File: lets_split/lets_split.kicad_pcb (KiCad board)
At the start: 2 copper layers, 112 x 79 mm, 62 parts, among them J1 3PIN, J2 6PIN, J3 3PIN, SW1 SW_PUSH, SW10 SW_PUSH, SW11 SW_PUSH, SW12 SW_PUSH, SW13 SW_PUSH, SW14 SW_PUSH, SW15 SW_PUSH, SW16 SW_PUSH, SW17 SW_PUSH, SW18 SW_PUSH, SW19 SW_PUSH, SW2 SW_PUSH, SW21 SW_PUSH, SW22 SW_PUSH, SW23 SW_PUSH, SW3 SW_PUSH, SW4 SW_PUSH, SW5 SW_PUSH, SW6 SW_PUSH, SW7 SW_PUSH, SW8 SW_PUSH, SW9 SW_PUSH, U2 HOLE, U3 HOLE, U4 HOLE, U5 HOLE

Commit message: Finished desing
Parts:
- removed ? (x2): SW_PUSH, flipalps:MXALPS_FLIP
- removed U2, U3, U4, U5: HOLE, prettylib:HOLE
- removed W1: TEST, prettylib:JUMPER_SMD_2DUB
- removed W2: TEST_1P, Wire_Pads:SolderWirePad_single_2mmDrill
- added JP1: I2C / Serial, Jumpers:Solder-jumper-NO, B.Cu at (157.6, 71.8)
- added REF**: 1pin, Connect:1pin, F.Cu at (186.2, 74.5)
- added REF**: 1pin, Connect:1pin, F.Cu at (186.3, 112.5)
- added REF**: 1pin, Connect:1pin, F.Cu at (110.0, 112.5)
- added SW20: SW_PUSH, Kailh-socket, F.Cu at (119.5, 122.0)
- added SW24: SW_PUSH, Kailh-socket, F.Cu at (195.8, 122.0)
- J1, J3: footprint prettylib:jumper -> jumper-3pin-smd-dualside
- J2: value 6PIN -> CONN_01X04; footprint footprint:4pin35mmAudio -> Connectors:4ucon-20153; moved to B.Cu
- R1, R2: value R -> 4k7; footprint footprint:RESISTOR -> Resistors_ThroughHole:R_Axial_DIN0207_L6.3mm_D2.5mm_P10.16mm_Horizontal
- SW1, SW10, SW11, SW12, SW13, SW14, SW15, SW16, SW17, SW18, SW19, SW2, SW21, SW22, SW23, SW3, SW4, SW5, SW6, SW7, SW8, SW9: footprint flipalps:MXALPS_FLIP -> Kailh-socket
- U1: value (none) -> ArduinoProMicro; footprint footprint:TEENSY_2.0 -> plug-in-modules:ArduinoProMicro; moved to F.Cu
- moved SW6 131.2 mm to (195.8, 64.8), turned to 180 degrees
- moved SW4 118.8 mm to (157.7, 64.8)
- moved SW12 113.9 mm to (195.8, 83.9), turned to 180 degrees
- moved SW5 113.6 mm to (176.7, 64.8), turned to 180 degrees
- moved SW3 95.3 mm to (138.6, 64.8)
- moved SW11 93.1 mm to (176.7, 83.9), turned to 180 degrees
- moved SW18 82.8 mm to (195.8, 103.0), turned to 180 degrees
- moved SW17 78.6 mm to (176.7, 103.0), turned to 180 degrees
- moved SW10 76.2 mm to (157.7, 83.9)
- moved SW21 75.2 mm to (138.6, 122.0), turned to 180 degrees
- moved SW2 74.0 mm to (119.5, 64.8), turned to 270 degrees
- moved SW9 66.3 mm to (138.6, 83.9)
- moved R1 62.6 mm to (156.3, 74.4)
- moved J2 60.4 mm to (186.9, 57.3)
- moved U1 59.6 mm to (120.3, 70.8)
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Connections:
- J2 pad 2: data -> SCL/D3
- J2 pad 3: xtradata -> SDA
- R1 pad 1: VCC -> Net-(JP1-Pad2)
- R1 pad 2: Net-(R1-Pad2) -> SDA
- R2 pad 1: data -> Net-(JP1-Pad2)
- R2 pad 2: VCC -> SCL/D3
- SW10 pad 1: col2 -> col3
- SW10 pad 2: Net-(D10-Pad2) -> Net-(D14-Pad2)
- SW11 pad 1: col2 -> col4
- SW11 pad 2: Net-(D11-Pad2) -> Net-(D18-Pad2)
- SW12 pad 1: col2 -> col5
- SW12 pad 2: Net-(D12-Pad2) -> Net-(D22-Pad2)
- SW13 pad 1: col3 -> col0
- SW13 pad 2: Net-(D13-Pad2) -> Net-(D3-Pad2)
- SW14 pad 1: col3 -> col1
- SW14 pad 2: Net-(D14-Pad2) -> Net-(D7-Pad2)
- SW15 pad 1: col3 -> col2
- SW15 pad 2: Net-(D15-Pad2) -> Net-(D11-Pad2)
- SW16 pad 2: Net-(D16-Pad2) -> Net-(D15-Pad2)
- SW17 pad 2: Net-(D17-Pad2) -> Net-(D19-Pad2)
- SW18 pad 1: col4 -> col5
- SW18 pad 2: Net-(D18-Pad2) -> Net-(D23-Pad2)
- SW19 pad 1: col4 -> col0
- SW19 pad 2: Net-(D19-Pad2) -> Net-(D4-Pad2)
- SW2 pad 1: col0 -> col1
- SW2 pad 2: Net-(D2-Pad2) -> Net-(D5-Pad2)
- SW21 pad 1: col5 -> col2
- SW21 pad 2: Net-(D21-Pad2) -> Net-(D12-Pad2)
- SW22 pad 1: col5 -> col3
- SW22 pad 2: Net-(D22-Pad2) -> Net-(D16-Pad2)
- SW23 pad 1: col5 -> col4
- SW23 pad 2: Net-(D23-Pad2) -> Net-(D20-Pad2)
- SW3 pad 1: col0 -> col2
- SW3 pad 2: Net-(D3-Pad2) -> Net-(D9-Pad2)
- SW4 pad 1: col0 -> col3
- SW4 pad 2: Net-(D4-Pad2) -> Net-(D13-Pad2)
- SW5 pad 1: col1 -> col4
- SW5 pad 2: Net-(D5-Pad2) -> Net-(D17-Pad2)
- SW6 pad 1: col1 -> col5
- SW6 pad 2: Net-(D6-Pad2) -> Net-(D21-Pad2)
- SW7 pad 1: col1 -> col0
- SW7 pad 2: Net-(D7-Pad2) -> Net-(D2-Pad2)
- SW8 pad 2: Net-(D8-Pad2) -> Net-(D6-Pad2)
- SW9 pad 2: Net-(D9-Pad2) -> Net-(D10-Pad2)
- U1 pad 10: col3 -> row2
- U1 pad 11: col4 -> row3
- U1 pad 12: col5 -> col1
- U1 pad 18: row3 -> Net-(U1-Pad18)
- U1 pad 19: row2 -> Net-(U1-Pad19)
- U1 pad 2: GND -> Net-(U1-Pad2)
- U1 pad 20: row1 -> Net-(U1-Pad20)
- U1 pad 21: row0 -> VCC
- U1 pad 23: Net-(U1-Pad23) -> GND
- U1 pad 24: data -> Net-(U1-Pad24)
- U1 pad 3: Net-(U1-Pad3) -> GND
- U1 pad 4: VCC -> GND
- U1 pad 5: Net-(U1-Pad5) -> SDA
- U1 pad 6: Net-(U1-Pad6) -> SCL/D3
- U1 pad 7: col0 -> row0
- U1 pad 8: col1 -> row1
- U1 pad 9: col2 -> col0
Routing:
- net data: track 117.5 -> 0.00 mm
- net SDA: track 0.00 -> 90.7 mm, vias 0 -> 2
- net SCL/D3: track 0.00 -> 87.0 mm, vias 0 -> 1
- net GND: track 15.8 -> 97.1 mm, vias 0 -> 1
- net Net-(R1-Pad2): track 77.0 -> 0.00 mm, vias 1 -> 0
- net VCC: track 27.2 -> 86.8 mm, vias 0 -> 1
- net col1: track 68.7 -> 103.6 mm
- net col0: track 96.5 -> 65.9 mm
- net col4: track 112.3 -> 141.5 mm, vias 0 -> 1
- net xtradata: track 25.8 -> 0.00 mm
- net Net-(D1-Pad2): track 27.6 -> 4.99 mm
- net col3: track 85.0 -> 103.3 mm, vias 0 -> 1
- net Net-(D3-Pad2): track 7.20 -> 24.8 mm, vias 0 -> 1
- net Net-(D5-Pad2): track 19.9 -> 2.96 mm
- net Net-(D19-Pad2): track 7.54 -> 24.2 mm
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- removed copper zone on F.Cu, net GND
- removed copper zone on B.Cu, net VCC
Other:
- board size 112 x 79 mm -> 113 x 78 mm
- net class Default: clearance 0.2 -> 0.1524; trace_width 0.25 -> 0.1524; via_dia 0.6 -> 0.8
- rule trace_clearance: 0.2 -> 0.1524
- rule trace_min: 0.2 -> 0.1524
- board text removed: "I2C"
- board text removed: "extra data"

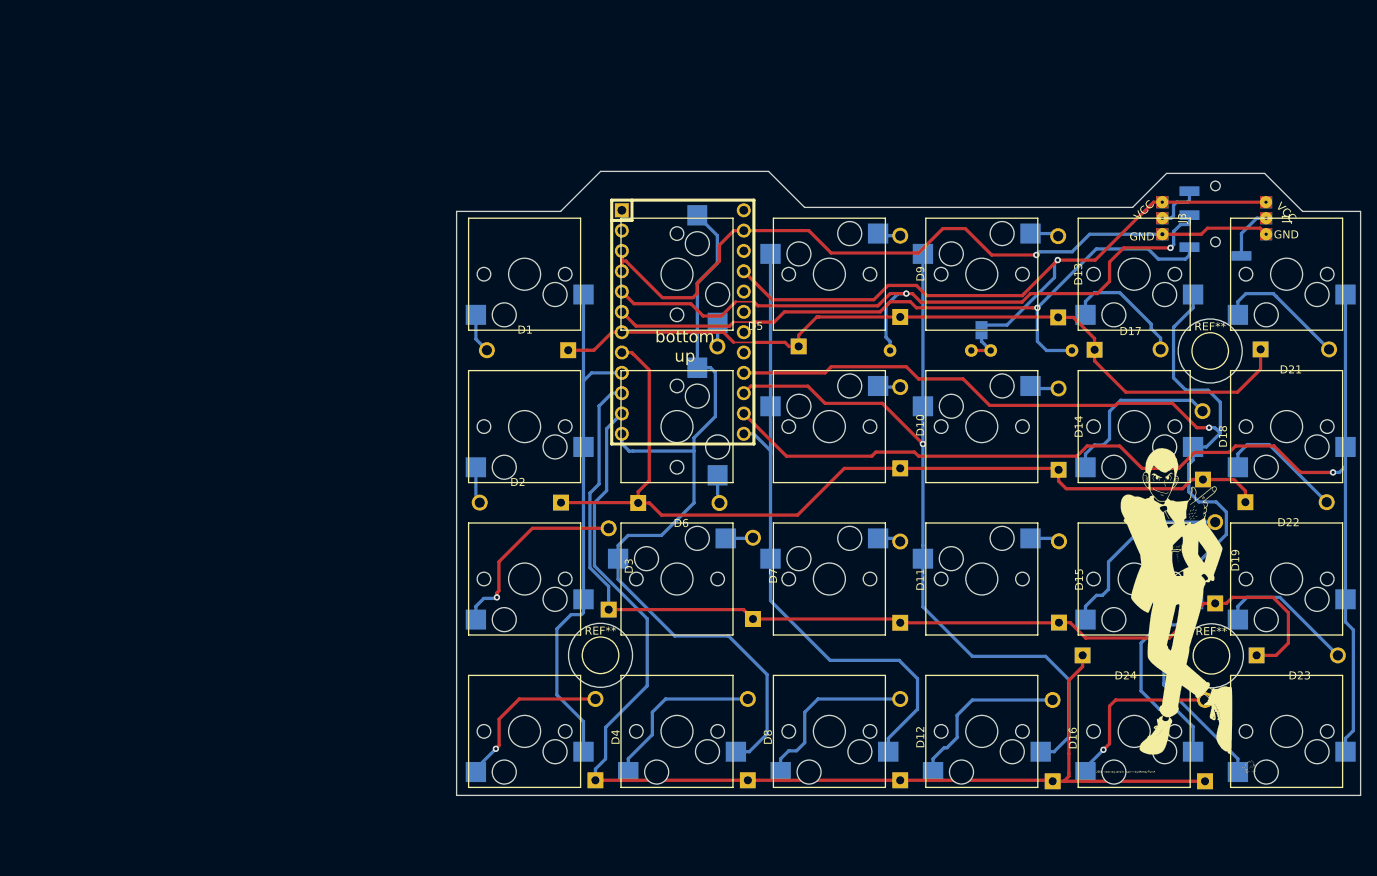
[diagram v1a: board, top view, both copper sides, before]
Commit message: Moved panel files into subfolder
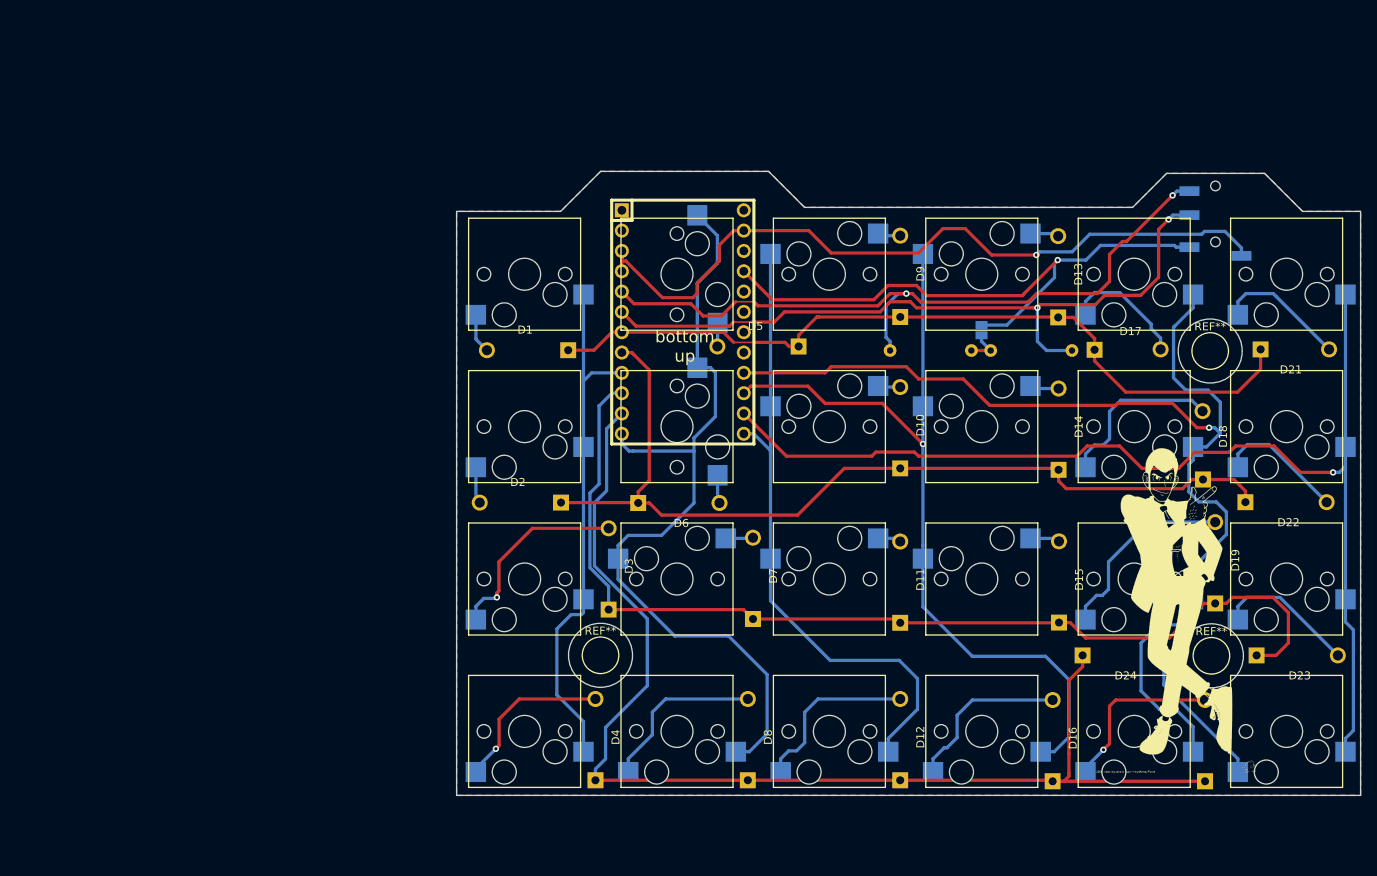
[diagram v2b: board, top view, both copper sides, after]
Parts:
- removed J1, J3: 3PIN, jumper-3pin-smd-dualside
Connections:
- J2 pad 1: Net-(J1-Pad2) -> GND
- J2 pad 2: SCL/D3 -> VCC
- J2 pad 3: SDA -> SCL/D3
- J2 pad 4: Net-(J2-Pad4) -> SDA
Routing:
- net VCC: track 86.8 -> 75.1 mm
- net Net-(J1-Pad2): track 6.69 -> 0.00 mm
- net Net-(J2-Pad4): track 6.24 -> 0.00 mm
- net SCL/D3: track 87.0 -> 91.1 mm, vias 1 -> 2
- net GND: track 97.1 -> 95.4 mm
- added copper zone on B.Cu, net GND
- added copper zone on F.Cu, net GND
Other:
- board text removed: "GND"
- board text removed: "VCC"

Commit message: V3 version, with mini usb added
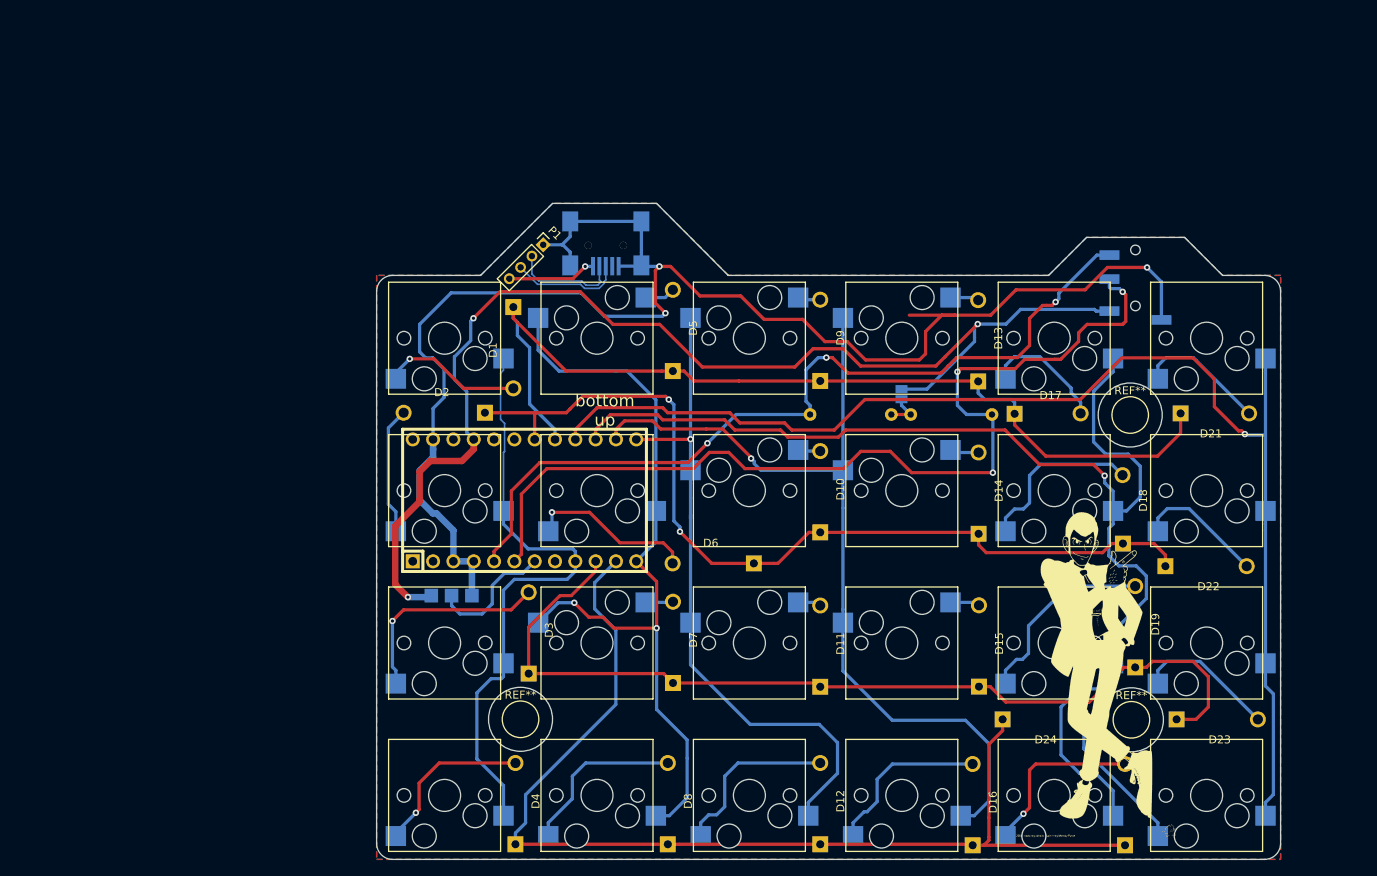
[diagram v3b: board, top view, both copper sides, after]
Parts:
- added P1: USB-rewire, Pin_Headers:Pin_Header_Straight_1x04_Pitch2.00mm, F.Cu at (102.8, 61.2)
- added P2: USB_OTG, Connectors:USB-Mini-B-SMD, B.Cu at (110.7, 60.0)
- added P3: WS2812-Strip, Pin_Headers:Pin_Header_Straight_1x03_Pitch2.54mm, B.Cu at (88.8, 105.0)
- moved U1 29.8 mm to (100.5, 93.1), turned to 0 degrees
- moved D6 16.3 mm to (129.2, 101.0), turned to 180 degrees
- moved D5 16.0 mm to (119.0, 77.0), turned to 90 degrees
- moved D2 14.7 mm to (95.5, 82.2)
- moved D7 12.8 mm to (119.0, 116.0)
- moved D10 12.8 mm to (137.5, 97.1)
- moved D11 12.8 mm to (137.5, 116.4)
- moved D12 12.8 mm to (137.5, 136.1)
- moved D13 12.8 mm to (157.2, 78.2)
- moved D14 12.8 mm to (157.2, 97.3)
- moved D15 12.8 mm to (157.3, 116.4)
- moved D16 12.8 mm to (156.5, 136.2)
- moved D17 12.8 mm to (161.8, 82.3)
- moved D18 12.8 mm to (175.3, 98.5)
- moved D19 12.8 mm to (176.8, 114.0)
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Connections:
- U1 pad 14: col5 -> col3
- U1 pad 15: col3 -> col4
- U1 pad 16: col4 -> col5
- U1 pad 17: Net-(U1-Pad17) -> row0
- U1 pad 18: Net-(U1-Pad18) -> row1
- U1 pad 7: row0 -> Net-(P3-Pad2)
- U1 pad 8: row1 -> Net-(U1-Pad8)
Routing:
- net GND: track 95.4 -> 196.3 mm, vias 1 -> 3
- net VCC: track 75.1 -> 150.5 mm, vias 1 -> 3
- net SCL/D3: track 91.1 -> 120.5 mm, vias 2 -> 3
- net Net-(D6-Pad2): track 3.55 -> 21.1 mm, vias 0 -> 1
- net col5: track 140.3 -> 157.5 mm
- net row0: track 99.8 -> 116.8 mm
- net Net-(P3-Pad2): track 0.00 -> 16.1 mm
- net /D-: track 0.00 -> 14.0 mm
- net SDA: track 90.9 -> 104.6 mm, vias 2 -> 3
- net /D+: track 0.00 -> 13.7 mm
- net Net-(D1-Pad2): track 4.99 -> 17.7 mm, vias 0 -> 1
- net row2: track 128.2 -> 116.1 mm
- net Net-(D2-Pad2): track 4.62 -> 16.0 mm
- net Net-(P1-Pad4): track 0.00 -> 11.1 mm, vias 0 -> 1
- net col4: track 141.5 -> 152.3 mm
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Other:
- board size 113 x 78 mm -> 113 x 82 mm
- board text added: "+ D -"

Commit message: Finished and panelized V3
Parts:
- added REF**: 1pin, Connect:1pin, F.Cu at (152.4, 82.5)
- added REF**: 1pin, Connect:1pin, F.Cu at (120.3, 75.2)
- added REF**: 1pin, Connect:1pin, F.Cu at (169.7, 78.2)
- added REF**: 1pin, Connect:1pin, F.Cu at (158.6, 73.4)
- added REF**: 1pin, Connect:1pin, F.Cu at (192.8, 76.2)
- added REF**: 1pin, Connect:1pin, F.Cu at (190.2, 98.0)
- added REF**: 1pin, Connect:1pin, F.Cu at (190.0, 116.6)
- added REF**: 1pin, Connect:1pin, F.Cu at (168.9, 124.0)
- added REF**: 1pin, Connect:1pin, F.Cu at (155.6, 129.5)
- added REF**: 1pin, Connect:1pin, F.Cu at (118.4, 128.8)
- added REF**: 1pin, Connect:1pin, F.Cu at (132.0, 127.8)
- added REF**: 1pin, Connect:1pin, F.Cu at (143.1, 82.6)
- added REF**: 1pin, Connect:1pin, F.Cu at (125.3, 113.8)
- added REF**: 1pin, Connect:1pin, F.Cu at (136.9, 110.6)
- added REF**: 1pin, Connect:1pin, F.Cu at (161.3, 68.6)
- added REF**: 1pin, Connect:1pin, F.Cu at (146.6, 85.7)
- added REF**: 1pin, Connect:1pin, F.Cu at (166.7, 84.5)
- added REF**: 1pin, Connect:1pin, F.Cu at (128.6, 97.7)
- added REF**: 1pin, Connect:1pin, F.Cu at (115.6, 88.1)
- added REF**: 1pin, Connect:1pin, F.Cu at (112.9, 90.1)
- added REF**: 1pin, Connect:1pin, F.Cu at (120.7, 103.3)
- added REF**: 1pin, Connect:1pin, F.Cu at (126.4, 105.3)
- P3: footprint Pin_Headers:Pin_Header_Straight_1x03_Pitch2.54mm -> SMD_PAD_1x03_Pitch2.54mm
- SW1, SW10, SW11, SW12, SW13, SW14, SW15, SW16, SW17, SW18, SW19, SW2, SW20, SW21, SW22, SW23, SW24, SW3, SW4, SW5, SW7, SW8, SW9: footprint Kailh-socket -> CherryMX:Kailh-socket
- moved D6 21.1 mm to (119.1, 82.4)
- moved U1 17.4 mm to (117.9, 93.1)
- moved P1 11.9 mm to (113.1, 67.1), turned to 270 degrees
- moved J2 4.47 mm to (173.9, 62.0)
- moved P3 3.33 mm to (87.5, 102.0)
- moved D5 1.89 mm to (118.1, 78.6)
- turned SW18 to 0 degrees
- turned SW2 to 180 degrees
- turned SW6 to 0 degrees
- turned SW9 to 180 degrees
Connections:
- P2 pad 2: /D+ -> /D-
- P2 pad 3: /D- -> /D+
- U1 pad 20: Net-(U1-Pad20) -> col0
- U1 pad 9: col0 -> Net-(U1-Pad9)
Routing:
- net GND: track 196.3 -> 137.2 mm
- net Net-(D10-Pad2): track 2.82 -> 25.3 mm, vias 0 -> 1
- net VCC: track 150.5 -> 128.5 mm
- net Net-(P3-Pad2): track 16.1 -> 35.8 mm, vias 0 -> 1
- net SCL/D3: track 120.5 -> 102.1 mm
- net col4: track 152.3 -> 134.1 mm
- net Net-(D5-Pad2): track 3.79 -> 20.4 mm
- net col3: track 110.4 -> 94.4 mm, vias 1 -> 2
- net row3: track 135.7 -> 148.8 mm
- net /D-: track 14.0 -> 3.56 mm
- net /D+: track 13.7 -> 3.44 mm
- net row0: track 116.8 -> 106.7 mm, vias 0 -> 1
- net col1: track 96.7 -> 106.7 mm, vias 2 -> 3
- net col2: track 83.6 -> 93.3 mm, vias 1 -> 0
- net row1: track 112.8 -> 103.4 mm, vias 2 -> 1
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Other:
- outline, holes or cut-outs redrawn
- rule trace_min: 0.1524 -> 0.006
- board text added: "- D +"
- board text added: "- D ~D~ +"
- board text added: "By Wootpatoot Socket Version by Duckle29"
- board text removed: "+ D -"
- board text removed: "By Wootpatoot"
